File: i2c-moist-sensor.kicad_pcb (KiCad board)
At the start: 2 copper layers, 18 x 149 mm, 25 parts, among them IC1 ATTINY441-SSU, P1 CONN_02X03, X1 16MHz

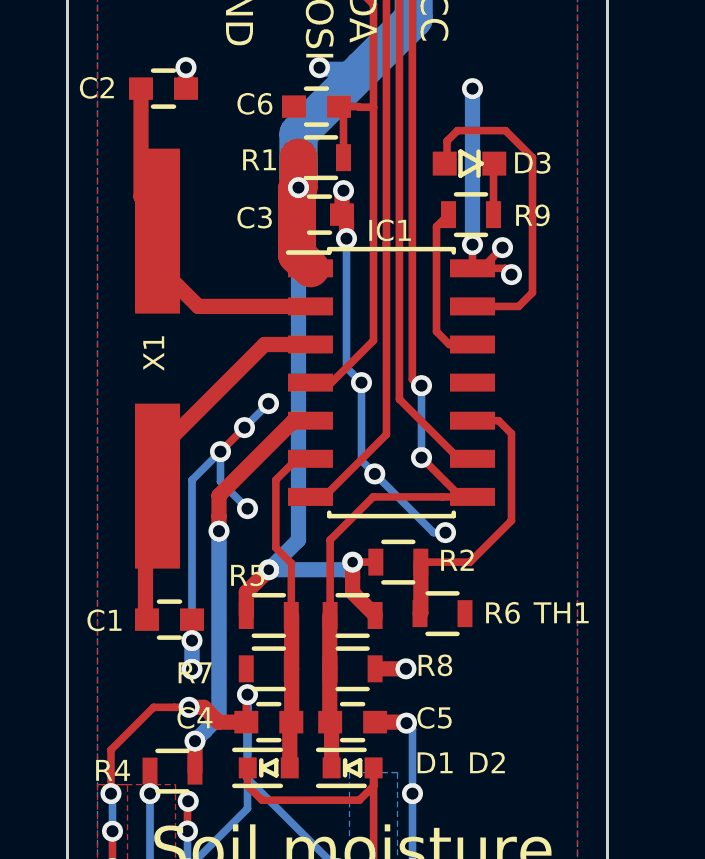
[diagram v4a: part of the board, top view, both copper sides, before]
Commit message: Power thermistor and moisture sensing circuitry from a pin rather than directly so lower the power consumption
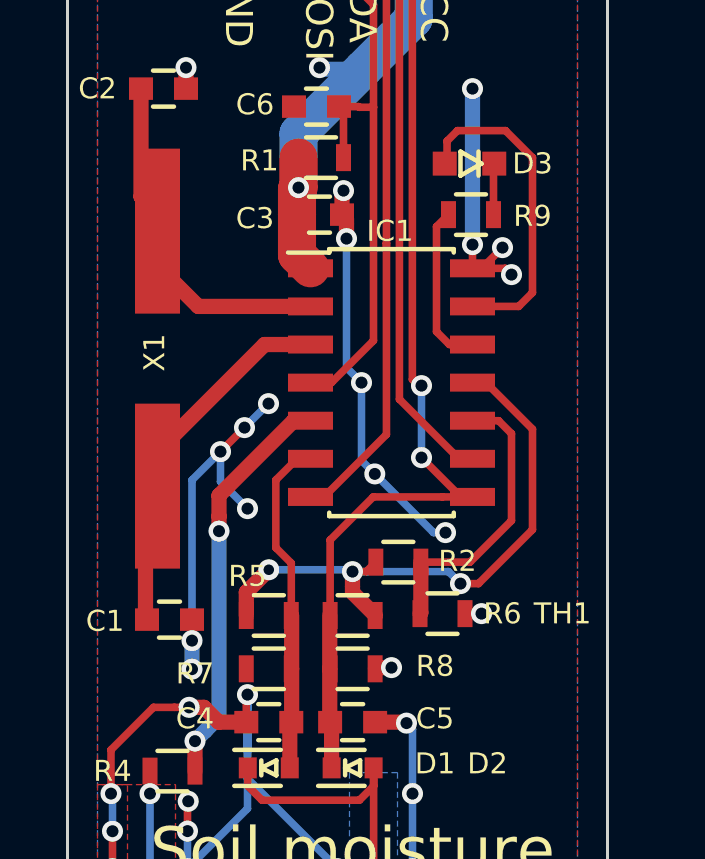
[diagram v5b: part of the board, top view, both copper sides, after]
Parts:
- C1: value 18p -> 33p
- C2: value 18p -> 33pp
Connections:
- R2 pad 1: VCC -> Net-(IC1-Pad11)
- R5 pad 2: VCC -> Net-(IC1-Pad11)
- R6 pad 2: VCC -> Net-(IC1-Pad11)
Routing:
- net VCC: track 37.2 -> 16.5 mm, vias 4 -> 2
- net Net-(IC1-Pad11): track 0.00 -> 20.2 mm, vias 0 -> 3
- net GND: track 223.7 -> 223.8 mm, vias 144 -> 145
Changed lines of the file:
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@@
-(kicad_pcb (version 20160815) (host pcbnew no-vcs-found-7518~57~ubuntu14.04.1)
+(kicad_pcb (version 20170123) (host pcbnew no-vcs-found-75cda50~59~ubuntu16.04.1)
   (general
-    (links 42)
-    (no_connects 0)
-    (area 85.949999 12.949999 104.050001 162.050001)
     (thickness 1.6)
     (drawings 20)
-    (tracks 462)
+    (tracks 474)
     (zones 0)
     (modules 25)
@@
       (effects (font (size 0.7 0.7) (thickness 0.11)))
     )
-    (fp_text value 18p (at -4.15 0.05) (layer F.Fab)
+    (fp_text value 33p (at -4.15 0.05) (layer F.Fab)
       (effects (font (size 0.7 0.7) (thickness 0.11)))
     )
@@
       (effects (font (size 0.7 0.7) (thickness 0.11)))
     )
-    (fp_text value 18p (at -4.45 0) (layer F.Fab)
+    (fp_text value 33pp (at -4.45 0) (layer F.Fab)
       (effects (font (size 0.7 0.7) (thickness 0.11)))
     )
@@
     (fp_line (start -0.5 -0.675) (end 0.5 -0.675) (layer F.SilkS) (width 0.15))
     (pad 1 smd rect (at -0.75 0) (size 0.5 0.9) (layers F.Cu F.Paste F.Mask)
-      (net 4 VCC))
+      (net 15 "Net-(IC1-Pad11)"))
     (pad 2 smd rect (at 0.75 0) (size 0.5 0.9) (layers F.Cu F.Paste F.Mask)
       (net 7 /THERMISTOR))
@@
       (net 5 /SENSE_LOW))
     (pad 2 smd rect (at 0.75 0 180) (size 0.5 0.9) (layers F.Cu F.Paste F.Mask)
-      (net 4 VCC))
+      (net 15 "Net-(IC1-Pad11)"))
     (model "${KIPRJMOD}/3d/User Library-RES_SMD-1.STEP"
       (at (xyz 0 0 0))
@@
       (net 14 /MISO/SENSE_HIGH))
     (pad 2 smd rect (at 0.75 0) (size 0.5 0.9) (layers F.Cu F.Paste F.Mask)
-      (net 4 VCC))
+      (net 15 "Net-(IC1-Pad11)"))
     (model "${KIPRJMOD}/3d/User Library-RES_SMD-1.STEP"
       (at (xyz 0 0 0))
@@
   (segment (start 88.6 51.65) (end 88.6 48.24886) (width 0.508) (layer F.Cu) (net 1))
   (segment (start 88.6 48.24886) (end 89 47.84886) (width 0.508) (layer F.Cu) (net 1))
+  (segment (start 96.30503 53.300004) (end 96.800004 53.300004) (width 0.508) (layer F.Cu) (net 2))
+  (segment (start 96.266 53.339034) (end 96.30503 53.300004) (width 0.508) (layer F.Cu) (net 2))
+  (segment (start 96.266 53.34) (end 96.266 53.339034) (width 0.508) (layer F.Cu) (net 2))
+  (via (at 96.800004 53.300004) (size 0.7) (drill 0.4) (layers F.Cu B.Cu) (net 2))
+  (segment (start 99.25 51.5) (end 99.8 51.5) (width 0.254) (layer F.Cu) (net 2))
+  (via (at 99.8 51.5) (size 0.7) (drill 0.4) (layers F.Cu B.Cu) (net 2))
   (segment (start 90 58.75) (end 90 57.779708) (width 0.254) (layer F.Cu) (net 2))
   (segment (start 90 57.779708) (end 90.024757 57.754951) (width 0.254) (layer F.Cu) (net 2))
@@
   (segment (start 90.15 51.7) (end 90.15 52.4) (width 0.254) (layer F.Cu) (net 2))
   (via (at 90.15 52.4) (size 0.7) (drill 0.4) (layers F.Cu B.Cu) (net 2))
-  (via (at 97.282 53.34) (size 0.7) (drill 0.4) (layers F.Cu B.Cu) (net 2))
-  (segment (start 96.266 53.34) (end 97.282 53.34) (width 0.508) (layer F.Cu) (net 2))
   (segment (start 88.45 34) (end 88.45 37.60114) (width 0.508) (layer F.Cu) (net 3))
   (segment (start 88.45 37.60114) (end 89 38.15114) (width 0.508) (layer F.Cu) (net 3))
@@
   (segment (start 89 39.9012) (end 89 38.15114) (width 0.508) (layer F.Cu) (net 3))
   (segment (start 89.06886 38.22) (end 89 38.15114) (width 0.254) (layer F.Cu) (net 3))
-  (segment (start 93.7 37.3) (end 93.7 49.048) (width 0.508) (layer B.Cu) (net 4))
-  (segment (start 93.7 49.048) (end 92.71 50.038) (width 0.508) (layer B.Cu) (net 4))
   (segment (start 95.846688 33.353312) (end 93.7 35.5) (width 1.27) (layer B.Cu) (net 4))
   (segment (start 97.54 31.66) (end 95.846688 33.353312) (width 1.27) (layer B.Cu) (net 4))
@@
   (segment (start 94.1 39.99) (end 93.65 39.54) (width 1.27) (layer F.Cu) (net 4))
   (segment (start 93.65 39.54) (end 93.65 38.2) (width 1.27) (layer F.Cu) (net 4))
-  (via (at 92.71 50.038) (size 0.7) (layers F.Cu B.Cu) (net 4))
-  (via (at 95.504 49.784) (size 0.7) (layers F.Cu B.Cu) (net 4))
-  (segment (start 95.25 50.038) (end 95.504 49.784) (width 0.508) (layer B.Cu) (net 4))
-  (segment (start 92.71 50.038) (end 95.25 50.038) (width 0.508) (layer B.Cu) (net 4))
-  (segment (start 91.96 50.788) (end 91.96 51.562) (width 0.508) (layer F.Cu) (net 4))
-  (segment (start 92.71 50.038) (end 91.96 50.788) (width 0.508) (layer F.Cu) (net 4))
-  (segment (start 96.266 51.562) (end 95.504 50.8) (width 0.508) (layer F.Cu) (net 4))
-  (segment (start 95.504 50.8) (end 95.504 50.278974) (width 0.508) (layer F.Cu) (net 4))
-  (segment (start 95.504 50.278974) (end 95.504 49.784) (width 0.508) (layer F.Cu) (net 4))
-  (segment (start 95.504 49.784) (end 96.278 49.784) (width 0.254) (layer F.Cu) (net 4))
+  (segment (start 95.5 50.1) (end 95.962 50.1) (width 0.254) (layer F.Cu) (net 15))
+  (segment (start 95.962 50.1) (end 96.278 49.784) (width 0.254) (layer F.Cu) (net 15))
+  (segment (start 96.266 51.562) (end 95.5 50.796) (width 0.508) (layer F.Cu) (net 15))
+  (segment (start 95.5 50.796) (end 95.5 50.594974) (width 0.508) (layer F.Cu) (net 15))
+  (segment (start 95.994974 50.1) (end 95.5 50.1) (width 0.254) (layer B.Cu) (net 15))
+  (segment (start 95.5 50.594974) (end 95.5 50.1) (width 0.508) (layer F.Cu) (net 15))
+  (segment (start 98.7 50.1) (end 95.994974 50.1) (width 0.254) (layer B.Cu) (net 15))
+  (segment (start 95.438 50.038) (end 95.5 50.1) (width 0.254) (layer B.Cu) (net 15))
+  (segment (start 92.71 50.038) (end 95.438 50.038) (width 0.254) (layer B.Cu) (net 15))
+  (segment (start 99.1 50.5) (end 98.7 50.1) (width 0.254) (layer B.Cu) (net 15))
+  (via (at 95.5 50.1) (size 0.7) (drill 0.4) (layers F.Cu B.Cu) (net 15))
+  (segment (start 101.5 48.7) (end 99.7 50.5) (width 0.254) (layer F.Cu) (net 15))
+  (segment (start 99.7 50.5) (end 99.1 50.5) (width 0.254) (layer F.Cu) (net 15))
+  (via (at 99.1 50.5) (size 0.7) (drill 0.4) (layers F.Cu B.Cu) (net 15))
+  (segment (start 101.5 45.35) (end 101.5 48.7) (width 0.254) (layer F.Cu) (net 15))
+  (segment (start 99.5 43.8) (end 99.95 43.8) (width 0.254) (layer F.Cu) (net 15))
+  (segment (start 99.95 43.8) (end 101.5 45.35) (width 0.254) (layer F.Cu) (net 15))
+  (via (at 92.71 50.038) (size 0.7) (layers F.Cu B.Cu) (net 15))
+  (segment (start 91.96 50.788) (end 91.96 51.562) (width 0.508) (layer F.Cu) (net 15))
+  (segment (start 92.71 50.038) (end 91.96 50.788) (width 0.508) (layer F.Cu) (net 15))
   (segment (start 93.8 38.35) (end 93.65 38.2) (width 0.508) (layer F.Cu) (net 4))
   (via (at 93.7 37.3) (size 0.7) (drill 0.4) (layers F.Cu B.Cu) (net 4))
@@
     )
     (polygon
-      (pts        (xy 99 148) (xy 99 95.3) (xy 91 95.3) (xy 91 148) (xy 93 150)
+      (pts
+        (xy 99 148) (xy 99 95.3) (xy 91 95.3) (xy 91 148) (xy 93 150)
         (xy 97 150) (xy 98 149)
       )

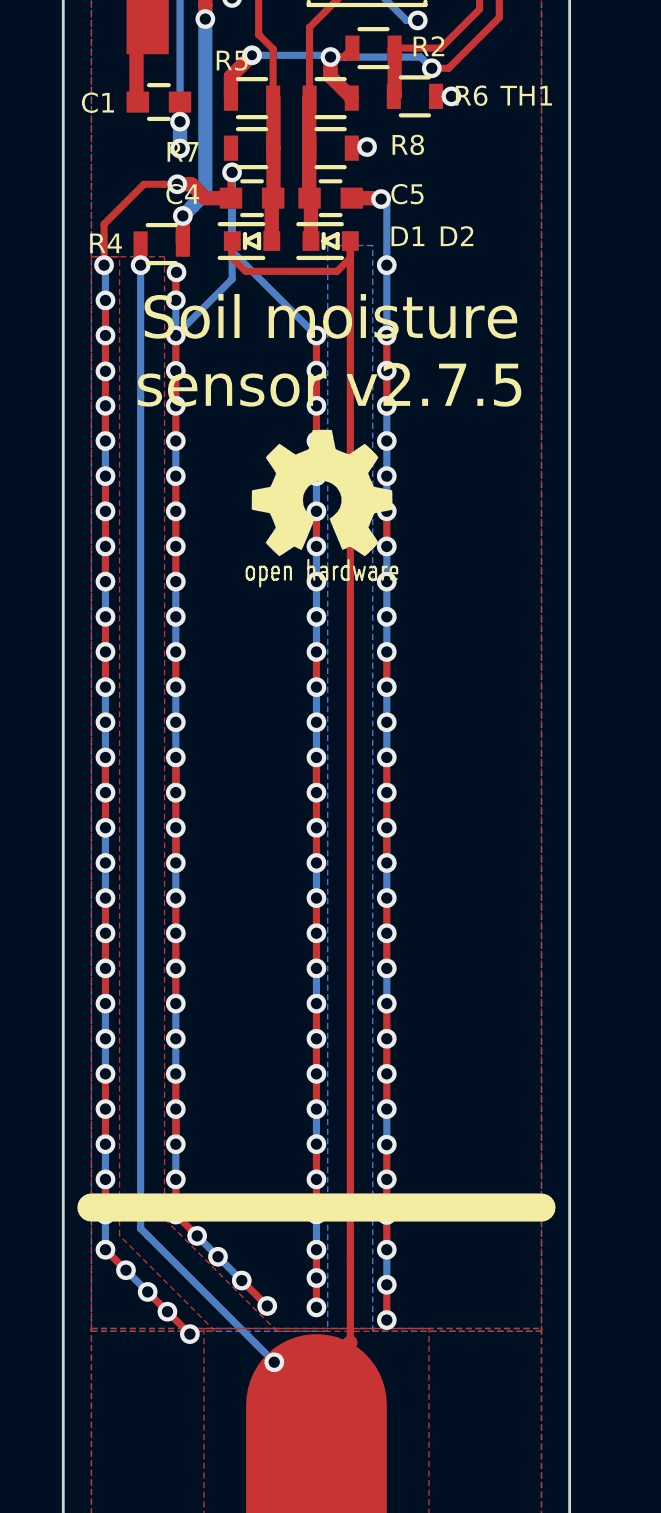
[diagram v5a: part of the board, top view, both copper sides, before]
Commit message: removed via's in earth
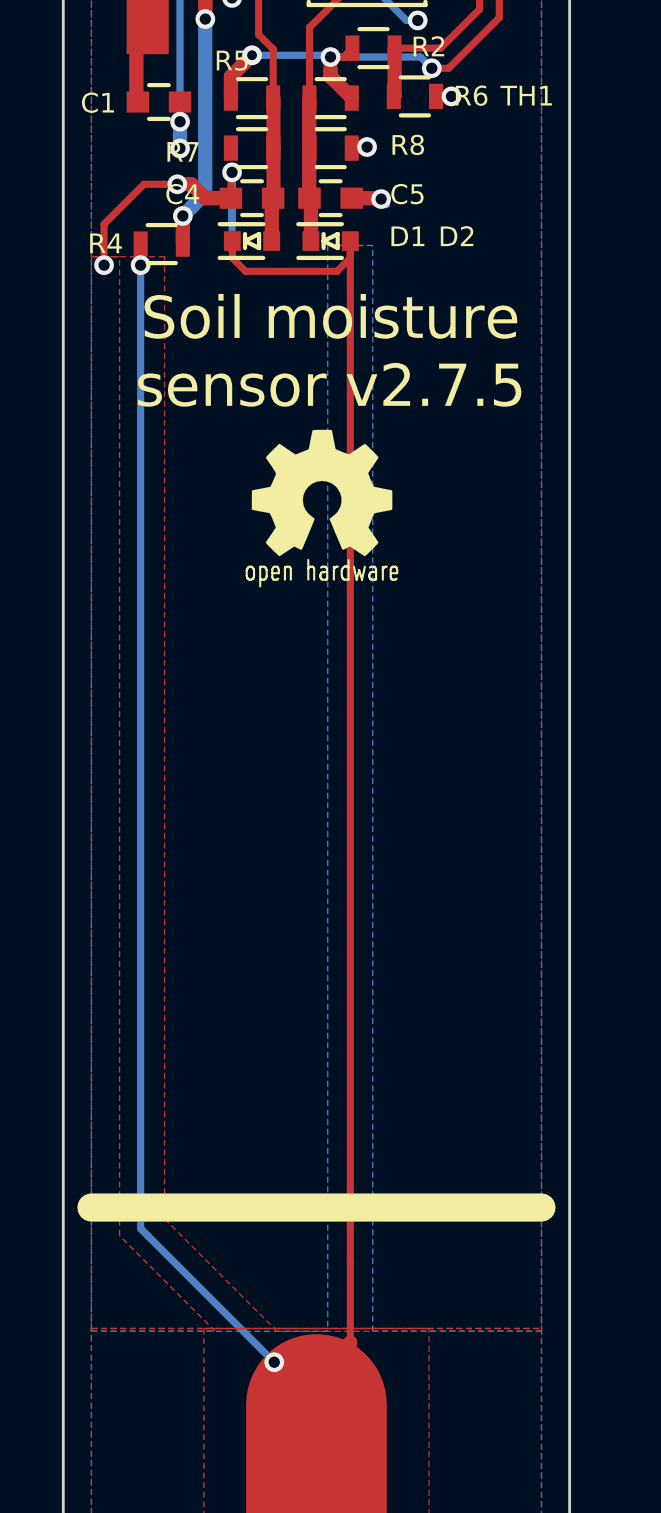
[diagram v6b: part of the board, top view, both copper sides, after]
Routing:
- net GND: track 223.8 -> 50.1 mm, vias 145 -> 22

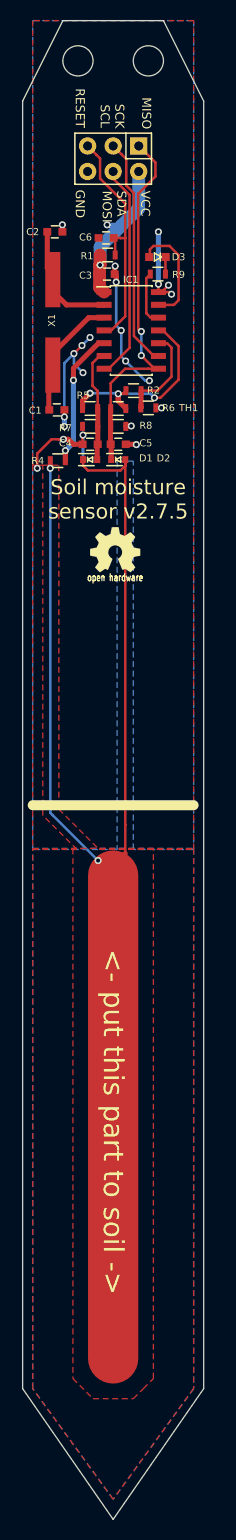
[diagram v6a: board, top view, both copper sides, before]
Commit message: 4 layers, B.Cu -> In2.Cu
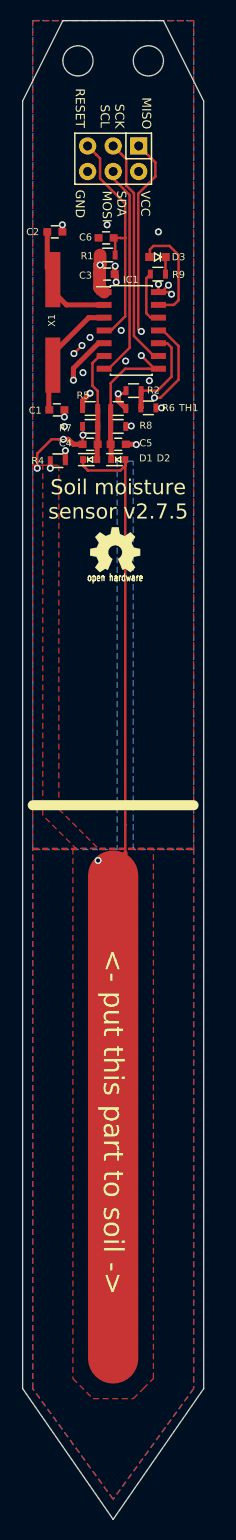
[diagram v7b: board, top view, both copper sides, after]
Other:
- copper layers 2 -> 4

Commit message: In1.Cu - sensing pad
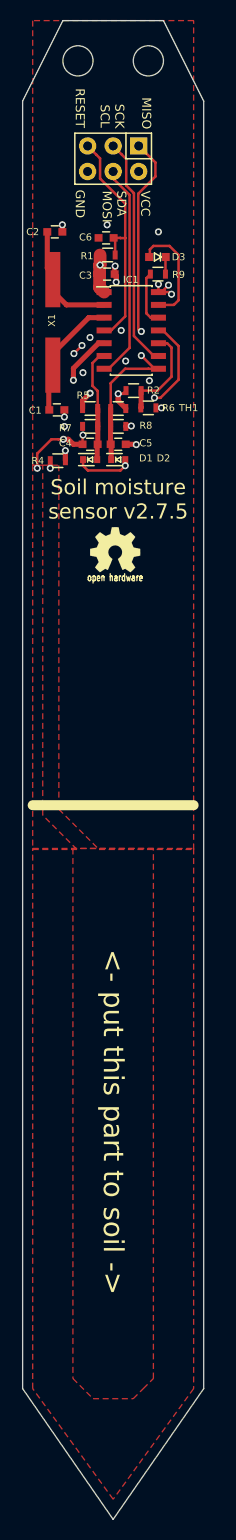
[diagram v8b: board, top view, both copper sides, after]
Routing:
- added copper zone on In2.Cu, net GND
- removed copper zone on B.Cu, net GND
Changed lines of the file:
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@@
     (thickness 1.6)
     (drawings 20)
-    (tracks 220)
+    (tracks 222)
     (zones 0)
     (modules 25)
@@
   (page A4)
   (layers
-    (0 F.Cu signal hide)
+    (0 F.Cu signal)
     (1 In1.Cu signal)
     (2 In2.Cu signal)
@@
   (segment (start 93.46 49.818894) (end 92.945199 49.304093) (width 0.254) (layer F.Cu) (net 5))
   (segment (start 93.46 51.562) (end 93.46 49.818894) (width 0.254) (layer F.Cu) (net 5))
-  (segment (start 88.75 91.75) (end 89 92) (width 0.254) (layer In2.Cu) (net 6))
-  (segment (start 89 92) (end 93.5 96.5) (width 0.254) (layer In2.Cu) (net 6))
-  (segment (start 93.5 96.5) (end 95 98) (width 0.254) (layer F.Cu) (net 6))
+  (segment (start 88.75 91.75) (end 89 92) (width 0.254) (layer In1.Cu) (net 6))
+  (segment (start 89 92) (end 93.5 96.5) (width 0.254) (layer In1.Cu) (net 6))
+  (segment (start 93.5 96.5) (end 95 98) (width 0.254) (layer In1.Cu) (net 6))
   (segment (start 96.204 56.642) (end 96.204 57.246) (width 0.254) (layer F.Cu) (net 6))
   (segment (start 96.204 57.246) (end 95.730999 57.719001) (width 0.254) (layer F.Cu) (net 6))
@@
   (segment (start 95.730999 57.719001) (end 92.483001 57.719001) (width 0.254) (layer F.Cu) (net 6))
   (segment (start 92.01 57.246) (end 92.01 56.642) (width 0.254) (layer F.Cu) (net 6))
-  (segment (start 96.204 95.796) (end 94.128468 97.871532) (width 0.508) (layer F.Cu) (net 6))
-  (segment (start 94.128468 97.871532) (end 94 98) (width 0.508) (layer F.Cu) (net 6))
-  (segment (start 95 98) (end 94.256936 98) (width 0.508) (layer F.Cu) (net 6))
-  (segment (start 94.256936 98) (end 94.128468 97.871532) (width 0.508) (layer F.Cu) (net 6))
-  (segment (start 88.75 57.5) (end 88.75 91.75) (width 0.254) (layer In2.Cu) (net 6))
-  (via (at 93.5 96.5) (size 0.7) (drill 0.4) (layers F.Cu B.Cu) (net 6))
+  (segment (start 96.204 95.796) (end 94.128468 97.871532) (width 0.508) (layer In1.Cu) (net 6))
+  (segment (start 94.128468 97.871532) (end 94 98) (width 0.508) (layer In1.Cu) (net 6))
+  (segment (start 95 98) (end 94.256936 98) (width 0.508) (layer In1.Cu) (net 6))
+  (segment (start 94.256936 98) (end 94.128468 97.871532) (width 0.508) (layer In1.Cu) (net 6))
+  (segment (start 88.75 57.5) (end 88.75 91.75) (width 0.254) (layer In1.Cu) (net 6))
   (segment (start 88.75 56.75) (end 88.75 57.5) (width 0.254) (layer F.Cu) (net 6))
   (via (at 88.75 57.5) (size 0.7) (drill 0.4) (layers F.Cu B.Cu) (net 6))
-  (segment (start 95 98) (end 95 146) (width 5) (layer F.Cu) (net 6))
-  (segment (start 96.204 56.642) (end 96.204 92.959962) (width 0.254) (layer F.Cu) (net 6))
-  (segment (start 96.204 92.959962) (end 96.204 95.796) (width 0.254) (layer F.Cu) (net 6))
+  (segment (start 95 98) (end 95 146) (width 5) (layer In1.Cu) (net 6))
+  (segment (start 96.204 56.642) (end 96.204 92.959962) (width 0.254) (layer In1.Cu) (net 6))
+  (segment (start 96.204 92.959962) (end 96.204 95.796) (width 0.254) (layer In1.Cu) (net 6))
+  (segment (start 96.204 57.023) (end 96.204 57.246) (width 0.254) (layer F.Cu) (net 6))
+  (segment (start 96.204 57.246) (end 96.204 57.023) (width 0.254) (layer F.Cu) (net 6))
+  (via (at 96.204 57.246) (size 0.7) (drill 0.4) (layers F.Cu B.Cu) (net 6))
   (segment (start 97.778 49.784) (end 97.778 51.472) (width 0.508) (layer F.Cu) (net 7))
   (segment (start 97.778 51.472) (end 97.75 51.5) (width 0.508) (layer F.Cu) (net 7))
@@
   (segment (start 98.3 42.1) (end 98.73 42.53) (width 0.254) (layer F.Cu) (net 16))
   (segment (start 98.73 42.53) (end 99.5 42.53) (width 0.254) (layer F.Cu) (net 16))
-  (zone (net 2) (net_name GND) (layer B.Cu) (hatch edge 0.508)
+  (zone (net 2) (net_name GND) (layer In2.Cu) (hatch edge 0.508)
     (connect_pads (clearance 0.254))
     (min_thickness 0.254)
@@
     (polygon
       (pts
-        (xy 103 149) (xy 95 160) (xy 87 149) (xy 87 95.3) (xy 103 95.3)
+        (xy 103 149) (xy 95 160) (xy 87 149) (xy 87 13) (xy 103 13)
+      )
+    )
+    (polygon
+      (pts
+        (xy 95.4 56.8) (xy 95.4 95.3) (xy 97 95.3) (xy 97 56.8)
       )
     )
@@
       )
     )
-  )
-  (zone (net 2) (net_name GND) (layer B.Cu) (hatch edge 0.508)
-    (connect_pads (clearance 0.254))
-    (min_thickness 0.254)
-    (fill yes (arc_segments 16) (thermal_gap 0.508) (thermal_bridge_width 0.508))
-    (polygon
-      (pts
-        (xy 103 95.4) (xy 97 95.4) (xy 97 56.8) (xy 95.4 56.8) (xy 95.4 95.4)
-        (xy 87 95.4) (xy 87 13) (xy 103 13)
-      )
-    )
